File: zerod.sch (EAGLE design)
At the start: 38 parts, among them IC1 NE5532N, IC2 LM3914N, Q1 2N3906

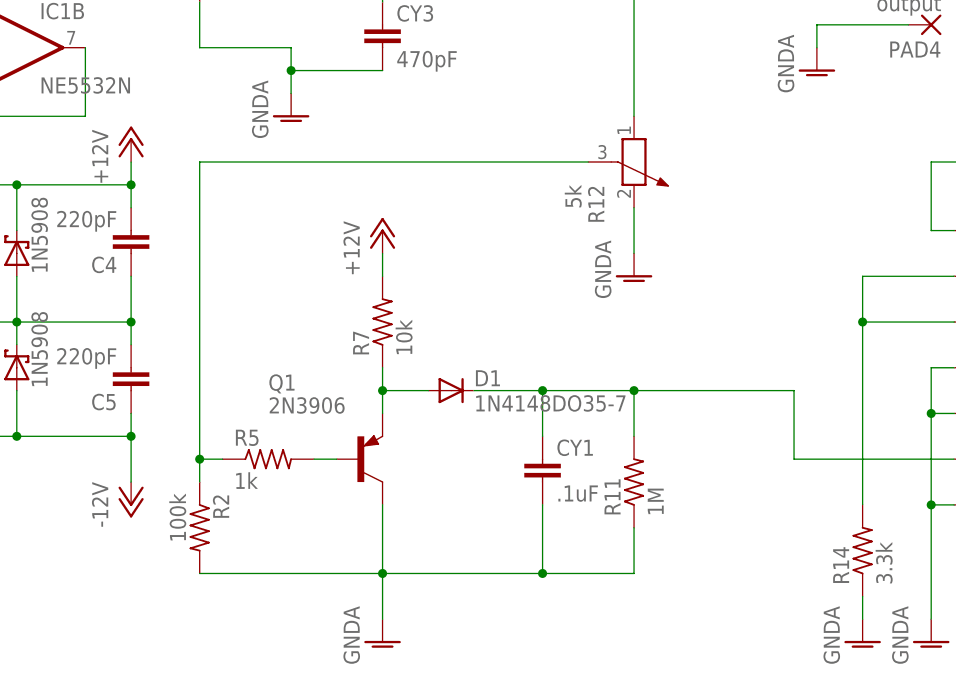
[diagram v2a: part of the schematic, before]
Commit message: ditching the peak finder circuit
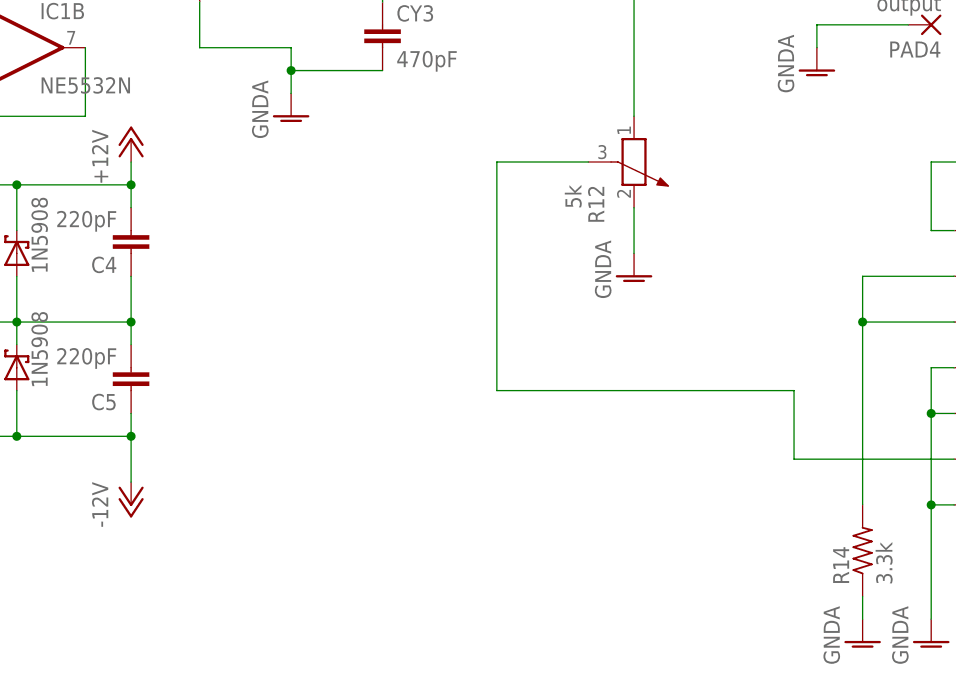
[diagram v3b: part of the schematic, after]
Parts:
- removed CY1: .1uF, rcl:CYYC7B5
- removed D1: 1N4148DO35-7, diode:1N4148DO35-7
- removed Q1: 2N3906, transistor-pnp:2N3906
- removed R11: 1M, rcl:R-US_0207/10
- removed R2: 100k, rcl:R-US_0207/10
- removed R5: 1k, rcl:R-US_0207/10
- removed R7: 10k, rcl:R-US_0207/10
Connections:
- removed net N$15: D1.A, Q1.E, R7.1
- removed net N$5: R12.3, R2.1, R5.1
- removed net N$9: Q1.B, R5.2
- net +12V: no longer R7.2
- net GNDA: no longer CY1.2, Q1.C, R11.1, R2.2
- net N$12: now also R12.3; no longer CY1.1, D1.C, R11.2
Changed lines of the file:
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@@
 <parts>
 <part name="C1" library="rcl" deviceset="CPOL-US" device="E15-6AXIAL" value="2.2uF"/>
-<part name="R7" library="rcl" deviceset="R-US_" device="0207/10" value="10k"/>
-<part name="R11" library="rcl" deviceset="R-US_" device="0207/10" value="1M"/>
-<part name="R2" library="rcl" deviceset="R-US_" device="0207/10" value="100k"/>
-<part name="R5" library="rcl" deviceset="R-US_" device="0207/10" value="1k"/>
 <part name="R15" library="rcl" deviceset="R-US_" device="0207/10" value="51"/>
 <part name="GND1" library="supply1" deviceset="GNDA" device=""/>
-<part name="P+1" library="supply1" deviceset="+12V" device=""/>
 <part name="P+2" library="supply1" deviceset="+12V" device=""/>
 <part name="IC1" library="linear" deviceset="NE5532" device="N"/>
@@
 <part name="PAD1" library="wirepad" deviceset="3,17/1,3" device="" value="input"/>
 <part name="PAD2" library="wirepad" deviceset="3,17/1,3" device="" value="output"/>
-<part name="Q1" library="transistor-pnp" deviceset="2N3906" device=""/>
-<part name="D1" library="diode" deviceset="1N4148" device="DO35-7"/>
-<part name="GND2" library="supply1" deviceset="GNDA" device=""/>
-<part name="CY1" library="rcl" deviceset="CY" device="YC7B5" value=".1uF"/>
 <part name="R12" library="rcl" deviceset="POTENTIOMETER_" device="PT-10S" value="5k"/>
 <part name="GND5" library="supply1" deviceset="GNDA" device=""/>
@@
 <instances>
 <instance part="C1" gate="G$1" x="10.16" y="81.28" rot="R90"/>
-<instance part="R7" gate="G$1" x="48.26" y="27.94" rot="R90"/>
-<instance part="R11" gate="G$1" x="76.2" y="10.16" rot="R90"/>
-<instance part="R2" gate="G$1" x="27.94" y="5.08" rot="R270"/>
-<instance part="R5" gate="G$1" x="35.56" y="12.7"/>
 <instance part="R15" gate="G$1" x="99.06" y="71.12"/>
 <instance part="GND1" gate="1" x="38.1" y="50.8"/>
-<instance part="P+1" gate="1" x="48.26" y="38.1"/>
 <instance part="P+2" gate="1" x="121.92" y="50.8"/>
 <instance part="IC1" gate="A" x="66.04" y="71.12" rot="MR180"/>
@@
 <instance part="PAD1" gate="1" x="-2.54" y="81.28"/>
 <instance part="PAD2" gate="1" x="109.22" y="71.12" rot="R180"/>
-<instance part="Q1" gate="G$1" x="45.72" y="12.7"/>
-<instance part="D1" gate="G$1" x="55.88" y="20.32"/>
-<instance part="GND2" gate="1" x="48.26" y="-7.62"/>
-<instance part="CY1" gate="G$1" x="66.04" y="12.7"/>
 <instance part="R12" gate="1" x="76.2" y="45.72" rot="R270"/>
 <instance part="GND5" gate="1" x="76.2" y="33.02"/>
@@
 <net name="GNDA" class="0">
 <segment>
-<pinref part="R2" gate="G$1" pin="2"/>
-<pinref part="GND2" gate="1" pin="GNDA"/>
-<wire x1="27.94" y1="0" x2="48.26" y2="0" width="0.1524" layer="91"/>
-<wire x1="48.26" y1="0" x2="48.26" y2="-5.08" width="0.1524" layer="91"/>
-<pinref part="Q1" gate="G$1" pin="C"/>
-<wire x1="48.26" y1="7.62" x2="48.26" y2="0" width="0.1524" layer="91"/>
-<junction x="48.26" y="0"/>
-<pinref part="CY1" gate="G$1" pin="2"/>
-<wire x1="66.04" y1="7.62" x2="66.04" y2="0" width="0.1524" layer="91"/>
-<wire x1="66.04" y1="0" x2="48.26" y2="0" width="0.1524" layer="91"/>
-<pinref part="R11" gate="G$1" pin="1"/>
-<wire x1="76.2" y1="5.08" x2="76.2" y2="0" width="0.1524" layer="91"/>
-<wire x1="76.2" y1="0" x2="66.04" y2="0" width="0.1524" layer="91"/>
-<junction x="66.04" y="0"/>
-</segment>
-<segment>
 <pinref part="GND5" gate="1" pin="GNDA"/>
 <pinref part="R12" gate="1" pin="2"/>
@@
 </segment>
 </net>
-<net name="N$5" class="0">
-<segment>
-<pinref part="R5" gate="G$1" pin="1"/>
-<wire x1="30.48" y1="12.7" x2="27.94" y2="12.7" width="0.1524" layer="91"/>
-<wire x1="27.94" y1="12.7" x2="27.94" y2="45.72" width="0.1524" layer="91"/>
-<pinref part="R2" gate="G$1" pin="1"/>
-<wire x1="27.94" y1="10.16" x2="27.94" y2="12.7" width="0.1524" layer="91"/>
-<junction x="27.94" y="12.7"/>
-<pinref part="R12" gate="1" pin="3"/>
-<wire x1="71.12" y1="45.72" x2="27.94" y2="45.72" width="0.1524" layer="91"/>
-</segment>
-</net>
 <net name="N$8" class="0">
 <segment>
@@
 </segment>
 </net>
-<net name="N$9" class="0">
-<segment>
-<pinref part="R5" gate="G$1" pin="2"/>
-<pinref part="Q1" gate="G$1" pin="B"/>
-<wire x1="40.64" y1="12.7" x2="43.18" y2="12.7" width="0.1524" layer="91"/>
-</segment>
-</net>
 <net name="N$12" class="0">
 <segment>
-<pinref part="CY1" gate="G$1" pin="1"/>
-<wire x1="66.04" y1="20.32" x2="66.04" y2="15.24" width="0.1524" layer="91"/>
-<pinref part="R11" gate="G$1" pin="2"/>
-<wire x1="76.2" y1="15.24" x2="76.2" y2="20.32" width="0.1524" layer="91"/>
-<wire x1="76.2" y1="20.32" x2="66.04" y2="20.32" width="0.1524" layer="91"/>
-<junction x="66.04" y="20.32"/>
-<wire x1="93.98" y1="20.32" x2="76.2" y2="20.32" width="0.1524" layer="91"/>
-<junction x="76.2" y="20.32"/>
-<pinref part="D1" gate="G$1" pin="C"/>
-<wire x1="58.42" y1="20.32" x2="66.04" y2="20.32" width="0.1524" layer="91"/>
+<wire x1="93.98" y1="20.32" x2="60.96" y2="20.32" width="0.1524" layer="91"/>
 <wire x1="93.98" y1="20.32" x2="93.98" y2="12.7" width="0.1524" layer="91"/>
 <pinref part="IC2" gate="A" pin="SIG"/>
 <wire x1="93.98" y1="12.7" x2="111.76" y2="12.7" width="0.1524" layer="91"/>
-</segment>
-</net>
-<net name="N$15" class="0">
-<segment>
-<pinref part="R7" gate="G$1" pin="1"/>
-<pinref part="Q1" gate="G$1" pin="E"/>
-<wire x1="48.26" y1="22.86" x2="48.26" y2="20.32" width="0.1524" layer="91"/>
-<wire x1="48.26" y1="20.32" x2="48.26" y2="17.78" width="0.1524" layer="91"/>
-<wire x1="53.34" y1="20.32" x2="48.26" y2="20.32" width="0.1524" layer="91"/>
-<junction x="48.26" y="20.32"/>
-<pinref part="D1" gate="G$1" pin="A"/>
+<pinref part="R12" gate="1" pin="3"/>
+<wire x1="71.12" y1="45.72" x2="60.96" y2="45.72" width="0.1524" layer="91"/>
+<wire x1="60.96" y1="45.72" x2="60.96" y2="20.32" width="0.1524" layer="91"/>
 </segment>
 </net>
 <net name="+12V" class="0">
 <segment>
-<pinref part="R7" gate="G$1" pin="2"/>
-<pinref part="P+1" gate="1" pin="+12V"/>
-<wire x1="48.26" y1="33.02" x2="48.26" y2="35.56" width="0.1524" layer="91"/>
-</segment>
-<segment>
 <pinref part="P+2" gate="1" pin="+12V"/>

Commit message: no peak finder and balanced
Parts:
- removed R15: 51, rcl:R-US_0207/10
- removed U$1: POWER, eurorack:POWER
- added C2: (no value), capacitor-wima:C2.5/6
- added R2, R7: 10k, rcl:R-US_0207/10
- added R5, R6: 150, rcl:R-US_0207/10
- added U$2: POWER_SIMPLE10, eurorack:POWER_SIMPLE10
- C6: device rcl:CPOL-USE22-6AXIAL -> rcl:CPOL-USE1.8-4
- PAD2: value output -> output TIP
- PAD4: value output -> output RING
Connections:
- removed net N$24: IC1B.-IN, IC1B.OUT
- new net N$15: PAD2.P, R5.2, R7.2
- new net N$5: PAD4.P, R6.2
- new net N$9: C2.2, IC1B.OUT, R5.1
- net +12V: now also U$2.+12V; no longer U$1.+12V
- net -12V: now also U$2.-12V; no longer U$1.-12V
- net GNDA: now also R6.1, U$2.GND; no longer PAD4.P, U$1.GND
- net N$3: now also R2.1; no longer R15.1
- net N$8: now also C2.1, IC1B.-IN, R2.2, R7.1; no longer PAD2.P, R15.2
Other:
- moved on the sheet: C3, CY3, IC1A, IC1B, PAD2, PAD4, R12

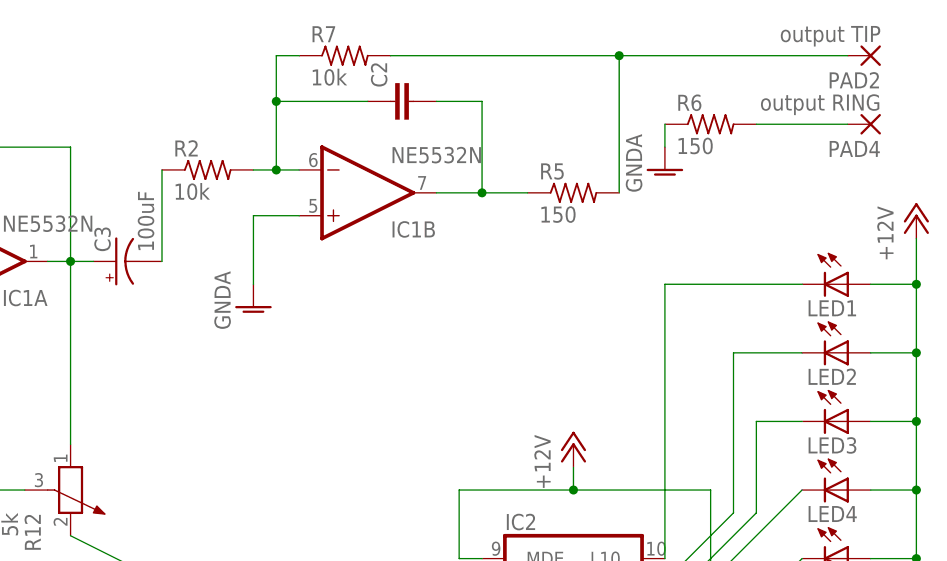
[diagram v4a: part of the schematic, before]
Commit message: value set for output filter cap
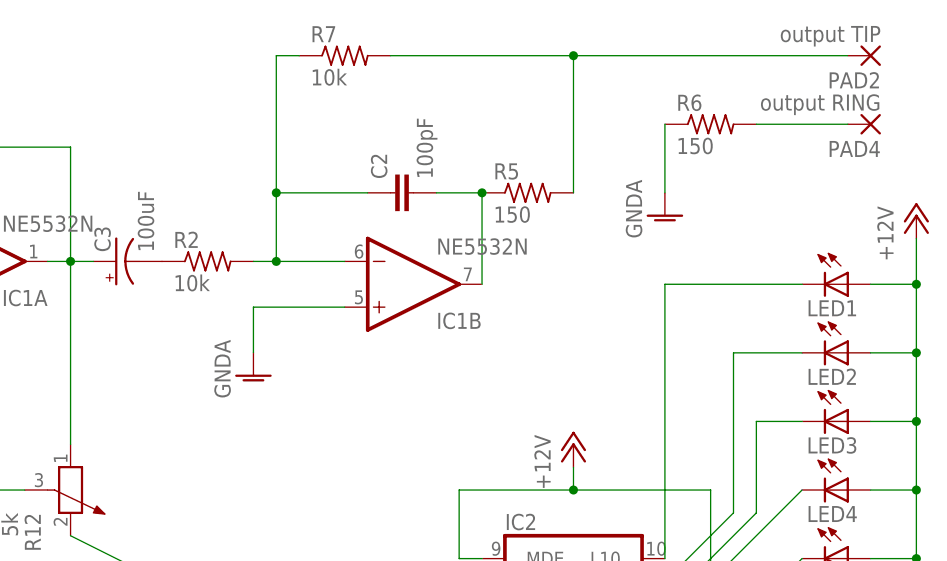
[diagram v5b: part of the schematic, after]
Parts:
- C2: value (none) -> 100pF
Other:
- moved on the sheet: C2, IC1B, R2, R5

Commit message: regen gcode with new schema
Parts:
- removed C3: 100uF, rcl:CPOL-USE22-6AXIAL
- R1, R4: value 5k -> 50k
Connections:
- removed net N$3: C3.-, R2.1
- net N$10: now also R2.1; no longer C3.+
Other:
- moved on the sheet: R2
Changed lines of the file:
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@@
 <part name="LED10" library="led" deviceset="LED" device="5MM"/>
 <part name="P+3" library="supply1" deviceset="+12V" device=""/>
-<part name="R1" library="rcl" deviceset="R-US_" device="0207/10" value="5k"/>
+<part name="R1" library="rcl" deviceset="R-US_" device="0207/10" value="50k"/>
 <part name="GND9" library="supply1" deviceset="GNDA" device=""/>
 <part name="P+4" library="supply1" deviceset="+12V" device=""/>
@@
 <part name="R3" library="rcl" deviceset="R-US_" device="0207/10" value="1k"/>
 <part name="CY3" library="rcl" deviceset="CY" device="YC7B5" value="470pF"/>
-<part name="R4" library="bourns" deviceset="91" device="" value="5k"/>
+<part name="R4" library="bourns" deviceset="91" device="" value="50k"/>
 <part name="PAD3" library="wirepad" deviceset="3,17/1,3" device="" value="input"/>
 <part name="GND4" library="supply1" deviceset="GNDA" device=""/>
@@
 <part name="D2" library="diode" deviceset="1N5908" device=""/>
 <part name="D3" library="diode" deviceset="1N5908" device=""/>
-<part name="C3" library="rcl" deviceset="CPOL-US" device="E22-6AXIAL" value="100uF"/>
 <part name="C6" library="rcl" deviceset="CPOL-US" device="E1.8-4" value="10uF"/>
 <part name="U$2" library="eurorack" deviceset="POWER_SIMPLE" device="10"/>
@@
 <instance part="D2" gate="1" x="7.62" y="35.56" rot="R90"/>
 <instance part="D3" gate="1" x="7.62" y="22.86" rot="R90"/>
-<instance part="C3" gate="G$1" x="71.12" y="71.12" rot="R90"/>
 <instance part="C6" gate="G$1" x="137.16" y="2.54"/>
 <instance part="U$2" gate="G$1" x="-17.78" y="40.64"/>
-<instance part="R2" gate="G$1" x="81.28" y="71.12"/>
+<instance part="R2" gate="G$1" x="78.74" y="71.12"/>
 <instance part="R5" gate="G$1" x="116.84" y="78.74"/>
 <instance part="R6" gate="G$1" x="137.16" y="86.36"/>
@@
 <segment>
 <pinref part="IC1" gate="A" pin="-IN"/>
-<pinref part="C3" gate="G$1" pin="+"/>
 <pinref part="IC1" gate="A" pin="OUT"/>
 <wire x1="63.5" y1="71.12" x2="66.04" y2="71.12" width="0.1524" layer="91"/>
 <junction x="66.04" y="71.12"/>
-<wire x1="66.04" y1="71.12" x2="68.58" y2="71.12" width="0.1524" layer="91"/>
 <wire x1="66.04" y1="83.82" x2="66.04" y2="71.12" width="0.1524" layer="91"/>
 <wire x1="48.26" y1="83.82" x2="66.04" y2="83.82" width="0.1524" layer="91"/>
@@
 <pinref part="R12" gate="1" pin="1"/>
 <wire x1="66.04" y1="50.8" x2="66.04" y2="71.12" width="0.1524" layer="91"/>
+<pinref part="R2" gate="G$1" pin="1"/>
+<wire x1="66.04" y1="71.12" x2="73.66" y2="71.12" width="0.1524" layer="91"/>
 </segment>
 </net>
@@
 <pinref part="IC1" gate="B" pin="-IN"/>
 <pinref part="R2" gate="G$1" pin="2"/>
-<wire x1="86.36" y1="71.12" x2="88.9" y2="71.12" width="0.1524" layer="91"/>
+<wire x1="83.82" y1="71.12" x2="88.9" y2="71.12" width="0.1524" layer="91"/>
 <pinref part="R7" gate="G$1" pin="1"/>
 <wire x1="88.9" y1="71.12" x2="96.52" y2="71.12" width="0.1524" layer="91"/>
@@
 </segment>
 </net>
-<net name="N$3" class="0">
-<segment>
-<pinref part="C3" gate="G$1" pin="-"/>
-<pinref part="R2" gate="G$1" pin="1"/>
-</segment>
-</net>
